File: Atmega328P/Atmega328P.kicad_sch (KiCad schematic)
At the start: 0 parts

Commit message: Added required Symbol
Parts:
- added BT1: Battery, symbol Device:Battery
- added C1: C_Polarized, symbol Device:C_Polarized
- added C2, C3, C4, C5: C, symbol Device:C
- added D1, D2: LED, symbol Device:LED
- added H1, H2, H3, H4: MountingHole, symbol Mechanical:MountingHole
- added R1, R2, R3, R4, R5, R6, R7: R, symbol Device:R
- added U1, U2: 24LC1025, symbol Memory_EEPROM:24LC1025
- added U3: DS1337S_, DS1337S_:SOIC127P600X175-8N, symbol DS1337S:DS1337S_
- added U4: ATMEGA328P-AU, ATMEGA328P-AU:QFP80P900X900X120-32N, symbol Atmega328P-AU:ATMEGA328P-AU
- added Y1, Y2: Crystal, symbol Device:Crystal
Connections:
- new net GND: U4.21 (GND), U4.3 (GND), U4.5 (GND)
- new net VCC: U4.4 (VCC), U4.6 (VCC)
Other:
- added sheet Connectors (Connectors_Sheet.kicad_sch)
- title: (none) -> ${Project Name}

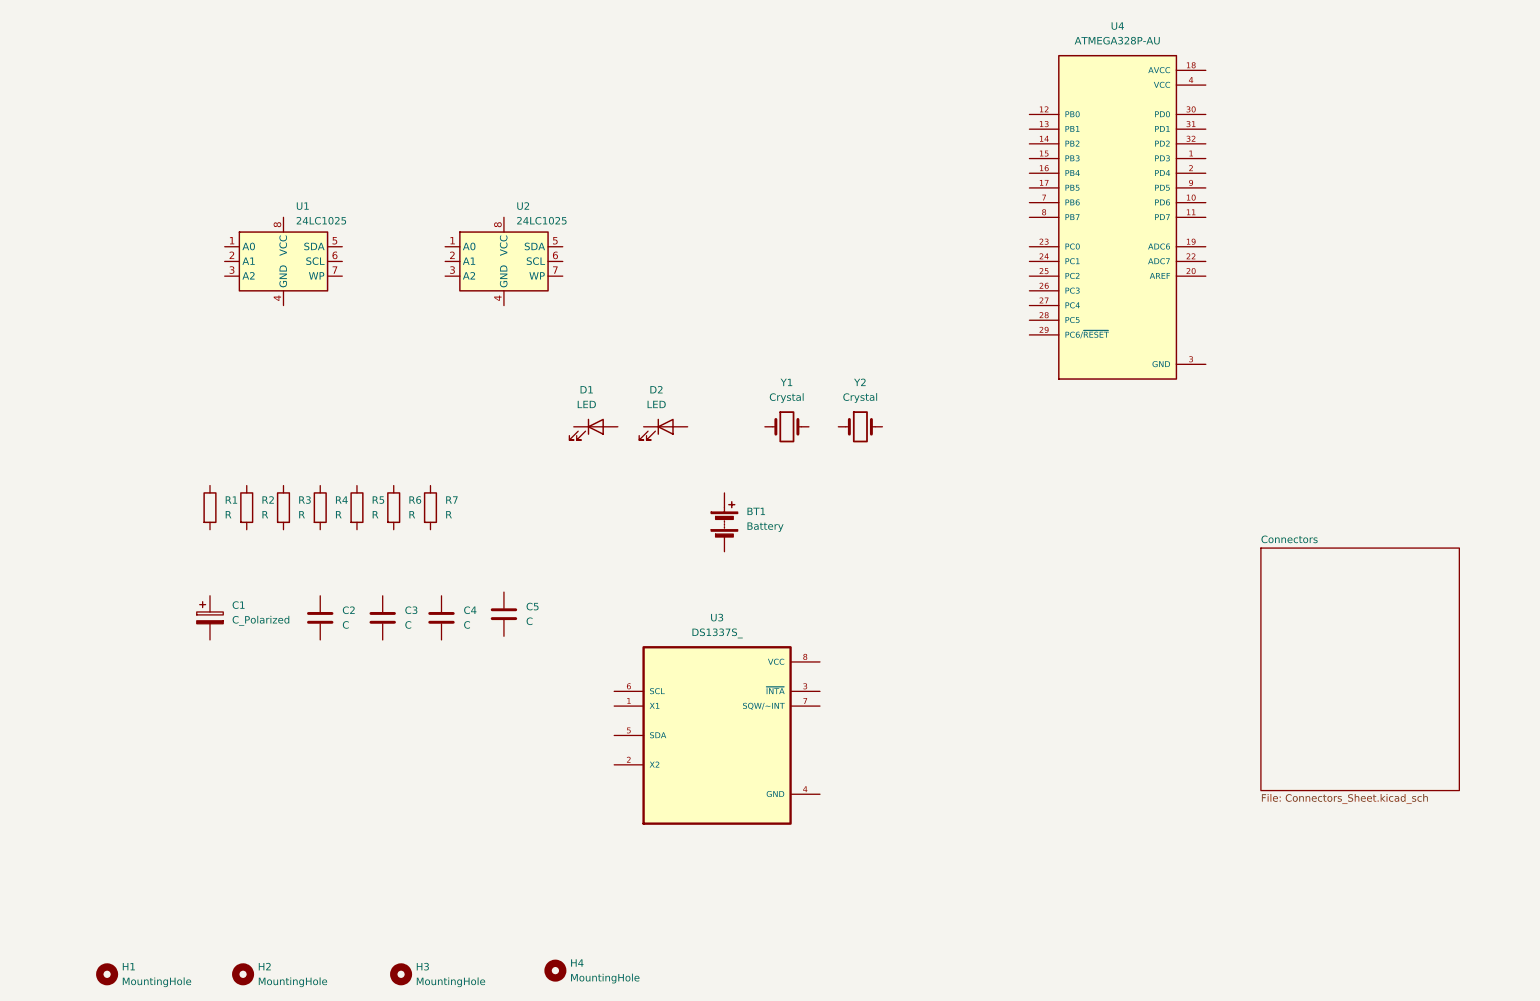
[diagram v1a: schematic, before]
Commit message: Componenets Value addded
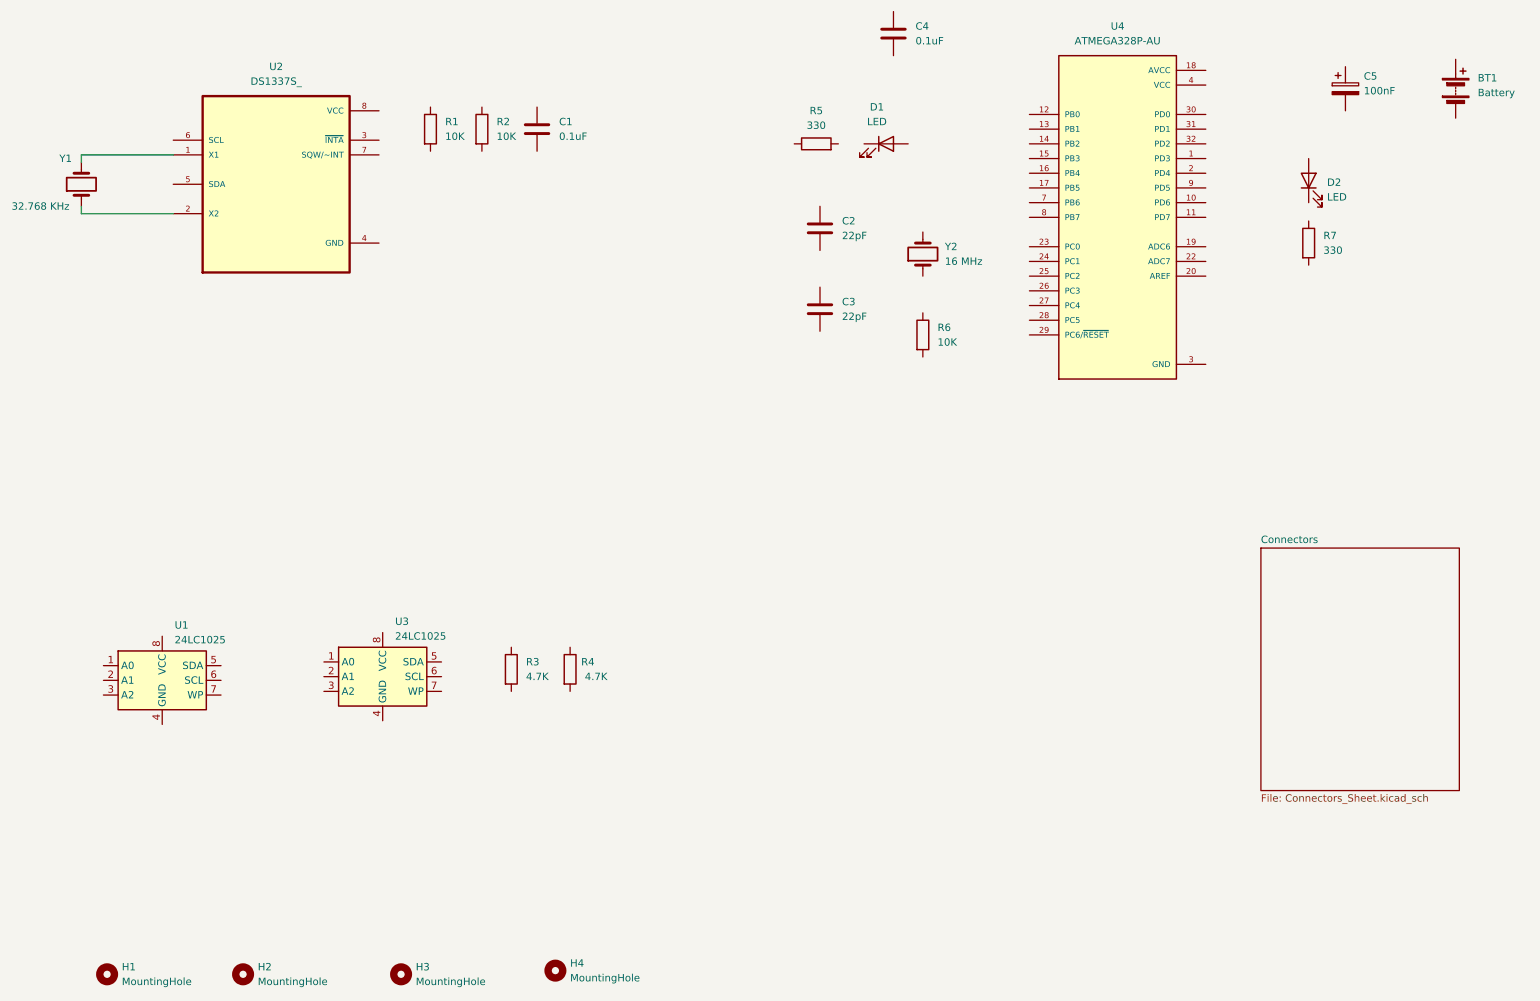
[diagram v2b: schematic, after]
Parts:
- C1: renamed from C5; value C -> 0.1uF
- C2: renamed from C3; value C -> 22pF
- C3: renamed from C2; value C -> 22pF
- C4: value C -> 0.1uF
- C5: renamed from C1; value C_Polarized -> 100nF
- R1: renamed from R6; value R -> 10K
- R2: renamed from R7; value R -> 10K
- R3: renamed from R4; value R -> 4.7K
- R4: renamed from R5; value R -> 4.7K
- R5: renamed from R3; value R -> 330
- R6: renamed from R2; value R -> 10K
- R7: renamed from R1; value R -> 330
- Y1: value Crystal -> 32.768 KHz
- Y2: value Crystal -> 16 MHz
- renumbered D2 to D1, D1 to D2, U3 to U2, U2 to U3
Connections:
- net at U2.1 (X1): now also Y1.2
- net at U2.2 (X2): now also Y1.1
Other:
- moved on the sheet: BT1, C1, C2, C3, C4, C5, D1, D2, R1, R2, R3, R4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

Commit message: Added the footprint for all symbols
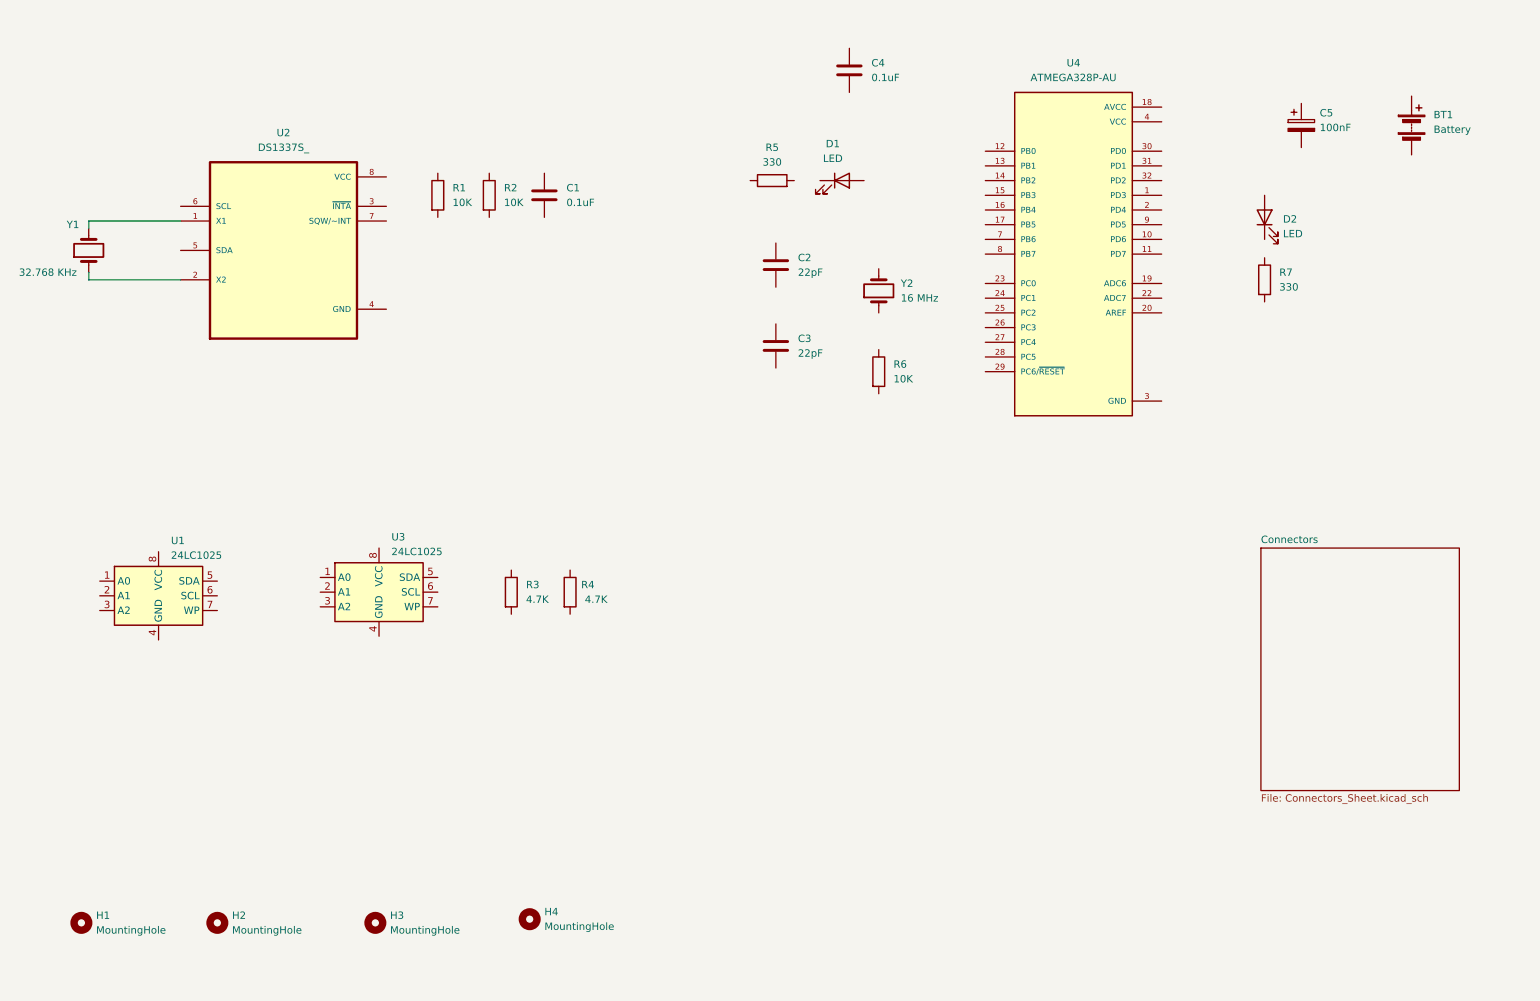
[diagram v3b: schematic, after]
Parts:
- BT1: footprint (none) -> Connector_PinHeader_2.54mm:PinHeader_1x02_P2.54mm_Vertical
- C1, C2, C3, C4, C5: footprint (none) -> Capacitor_SMD:C_0805_2012Metric
- D1, D2: footprint (none) -> LED_SMD:LED_0805_2012Metric
- H1, H2, H3, H4: footprint (none) -> MountingHole:MountingHole_2.2mm_M2
- R1, R2, R3, R4, R5, R6, R7: footprint (none) -> Resistor_SMD:R_0805_2012Metric
- U1, U3: footprint (none) -> Package_SO:SOIC-8_5.3x5.3mm_P1.27mm
- U2: footprint DS1337S_:SOIC127P600X175-8N -> KIcad_Footprint:DS1337S_SOIC127P600X175-8N
- U4: footprint ATMEGA328P-AU:QFP80P900X900X120-32N -> KIcad_Footprint:QFP80P900X900X120-32N
- Y1, Y2: footprint (none) -> Crystal:Crystal_SMD_5032-2Pin_5.0x3.2mm_HandSoldering
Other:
- moved on the sheet: BT1, C1, C2, C3, C4, C5, D1, D2, H1, H2, H3, H4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

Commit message: Completed Wiring
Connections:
- net GND: now also BT1.2 (-), C1.2, C2.1, C3.1, C4.2, C5.2, R5.1, R7.2, U1.4 (GND), U1.7 (WP), U2.4 (GND), U3.2 (A1), U3.4 (GND), U3.7 (WP)
- net VCC: now also BT1.1 (+), C1.1, C5.1, D2.2 (A), R1.1, R2.1, R3.1, R4.1, R6.1, U1.1 (A0), U1.2 (A1), U1.3 (A2), U1.8 (VCC), U2.8 (VCC), U3.1 (A0), U3.3 (A2), U3.8 (VCC), U4.18 (AVCC)
- net at C3.2: now also U4.8 (PB7), Y2.1
- net at D2.1 (K): now also R7.1
- net SDA: now reaches U1.5 (SDA)
- net SDA: now also R3.2, U2.5 (SDA), U3.5 (SDA), U4.27 (PC4)
- net SCL: now reaches U1.6 (SCL)
- net SCL: now also D1.2 (A), R4.2, U2.6 (SCL), U3.6 (SCL), U4.17 (PB5), U4.28 (PC5)
- net at Y2.2: now also C2.2, U4.7 (PB6)
- net at R2.2: now also U2.7 (SQW/~INT)
- net RESET: now reaches R6.2
- net RESET: now also U4.29 (PC6/~{RESET})
- net at D1.1 (K): now also R5.2
- net D3: now reaches U4.1 (PD3)
- net D6: now reaches U4.10 (PD6)
- net D7: now reaches U4.11 (PD7)
- net D8: now reaches U4.12 (PB0)
- net MOSI: now reaches U4.15 (PB3)
- net MISO: now reaches U4.16 (PB4)
- net D4: now reaches U4.2 (PD4)
- net at U4.20 (AREF): now also C4.1
- net RX: now reaches U4.30 (PD0)
- net TX: now reaches U4.31 (PD1)
- net D1: now reaches U4.32 (PD2)
- net D5: now reaches U4.9 (PD5)
- net at U2.3 (~{INTA}): now also R1.2
- no-connect marks 0 -> 8
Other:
- moved on the sheet: BT1, C2, C3, C4, C5, D1, R3, R4, R5, R6, Y2

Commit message: Routing completed
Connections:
- net D1 renamed D2
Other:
- sheet Connectors ports: added D2, D3, D4, D5, D6, D7, D8, GND, MISO, MOSI, RESET, RX, SCK, SCL, SDA, TX, Vcc; removed none

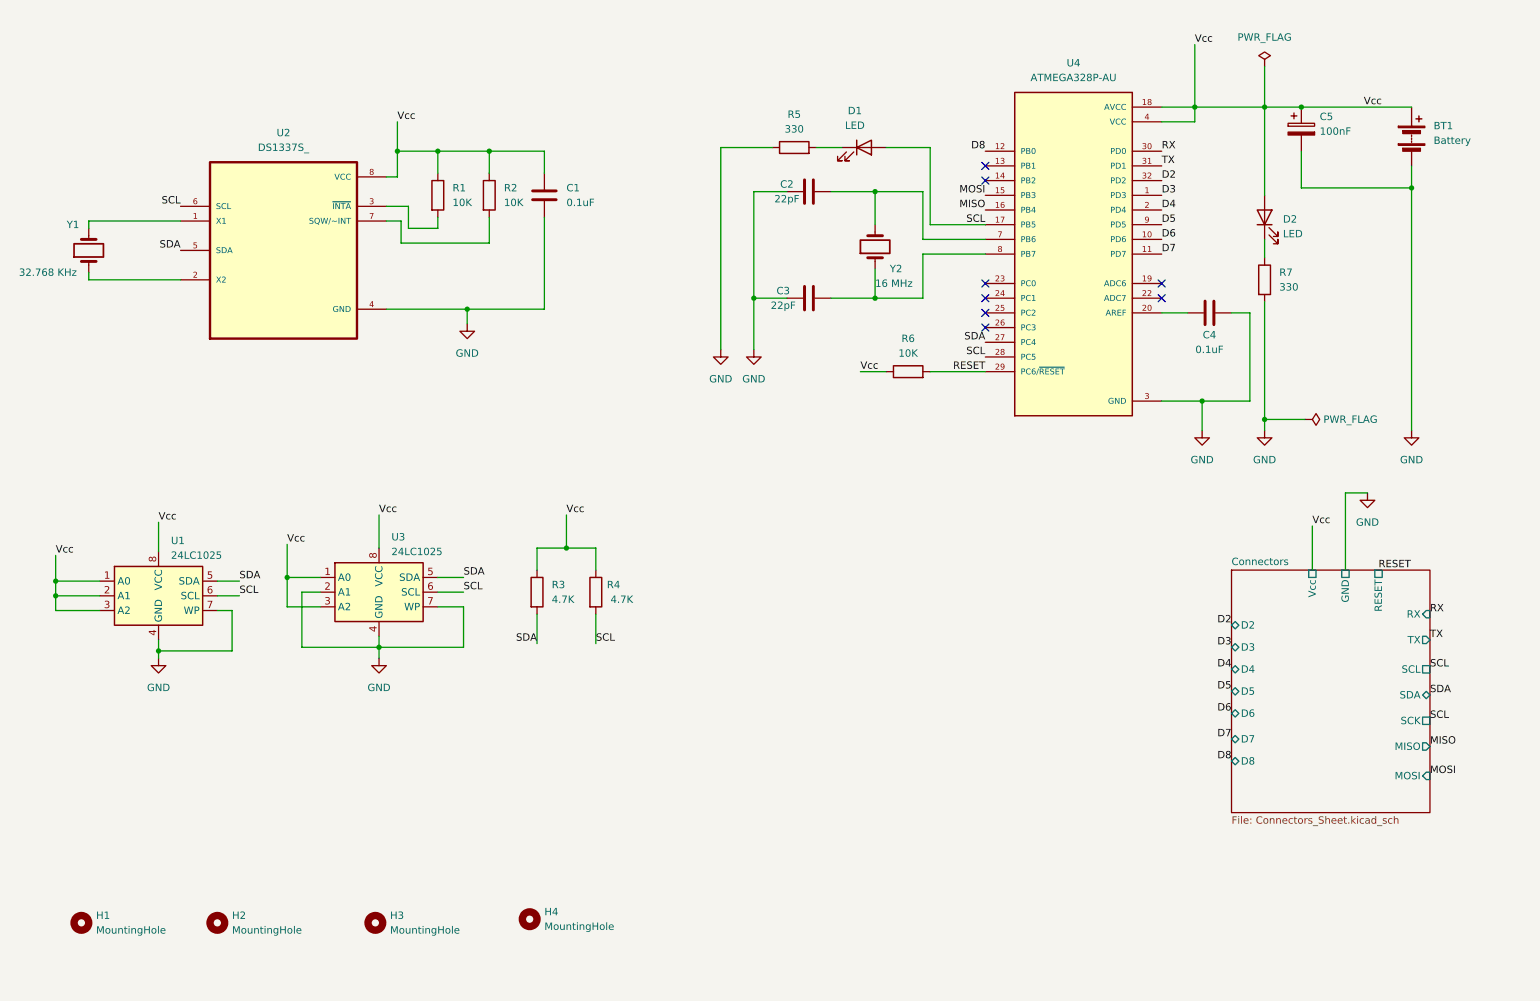
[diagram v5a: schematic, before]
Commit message: SCL Error - fixed
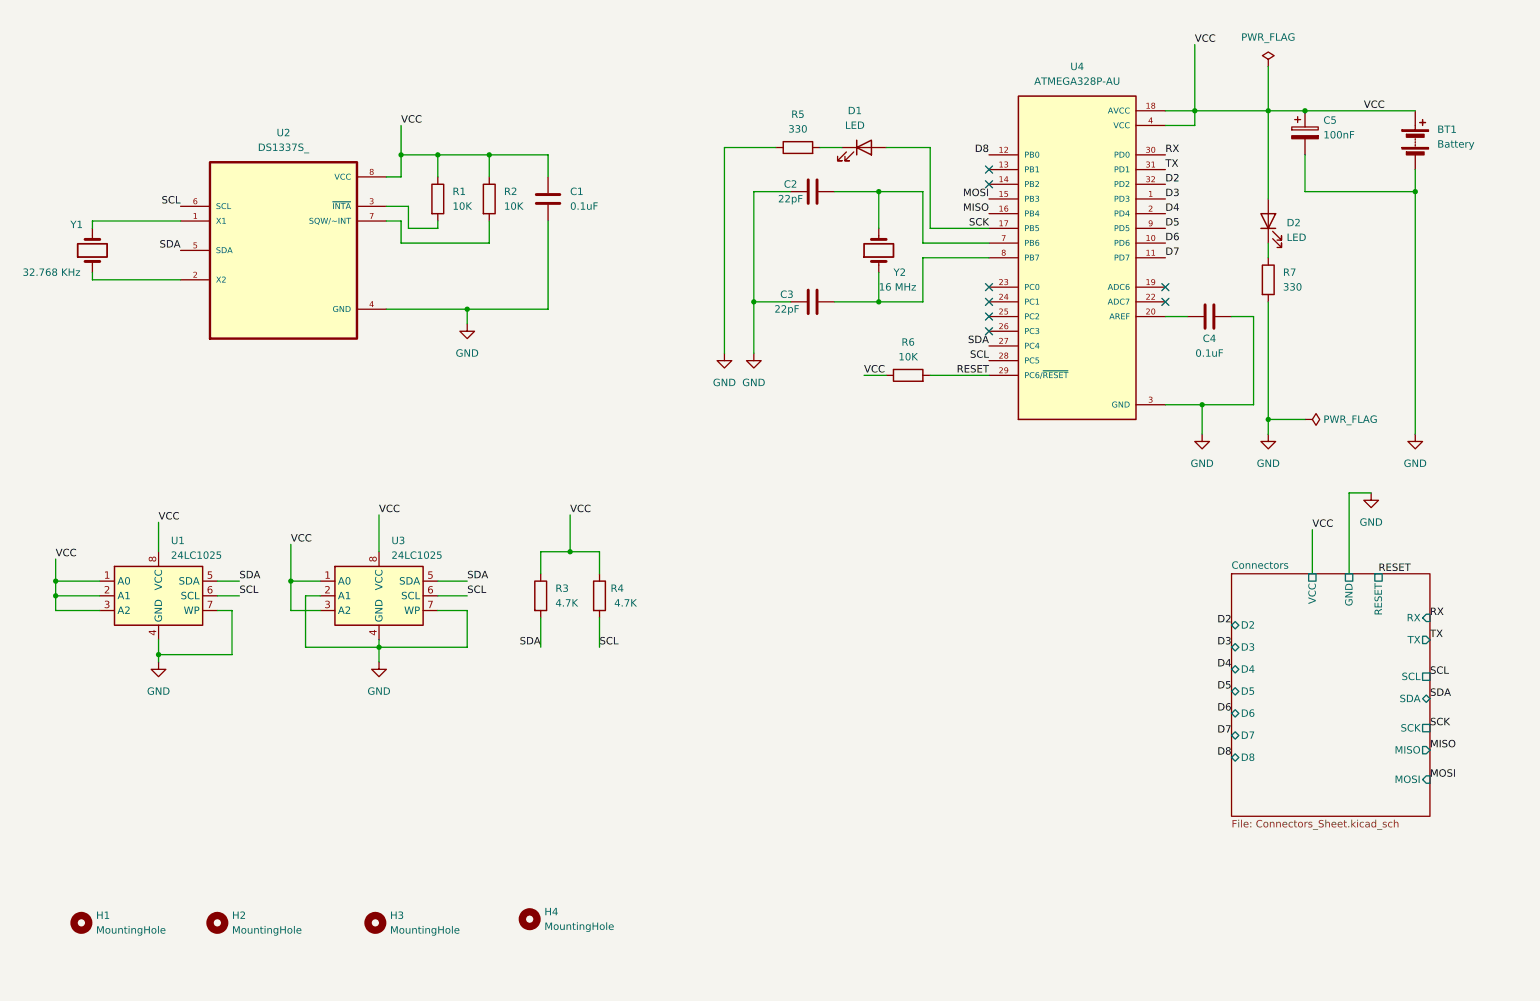
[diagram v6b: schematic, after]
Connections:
- net SCL: no longer D1.2 (A), U4.17 (PB5)
- new net SCK: D1.2 (A), U4.17 (PB5)
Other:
- sheet Connectors ports: added VCC; removed Vcc
- moved on the sheet: BT1, C1, C2, C3, C4, C5, D2, R1, R2, R3, R4, R5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
